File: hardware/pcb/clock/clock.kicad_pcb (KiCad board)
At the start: 2 copper layers, 32 parts, among them J1 01x02_F, J2 01x04_F, SW1 SW_Push, SW2 SW_SPDT, U1 TLC556, U3 74HC02, U4 74HC00

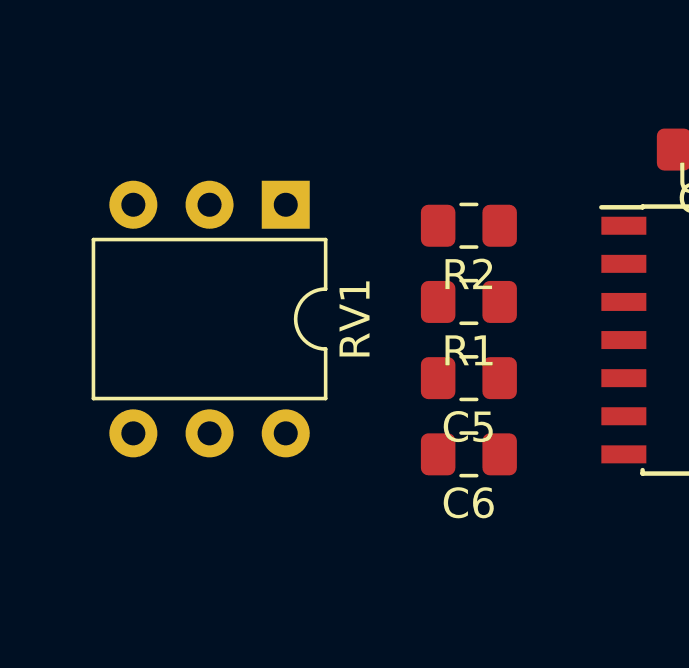
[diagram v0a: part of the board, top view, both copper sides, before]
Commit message: Custom footprints for non-standard parts
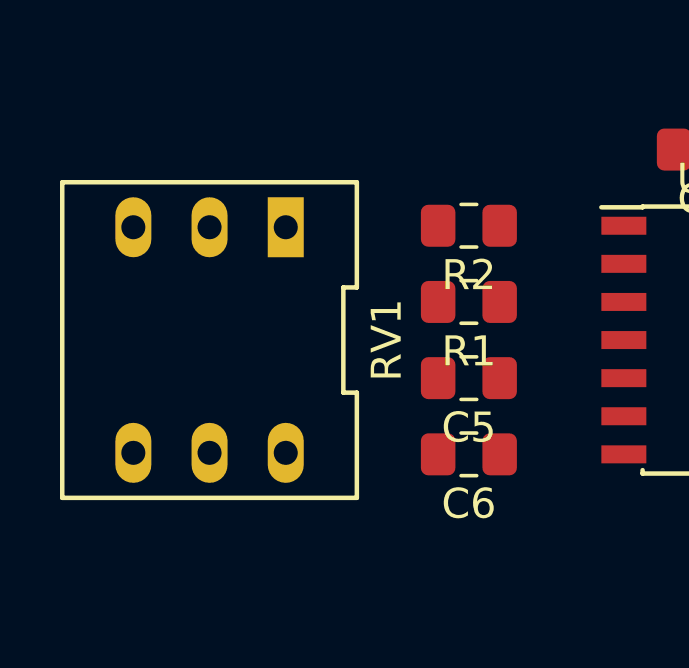
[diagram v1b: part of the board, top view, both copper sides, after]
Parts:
- RV1: footprint Package_DIP:DIP-6_W7.62mm -> clock-custom:POT_DIP_Dual_Vert
- SW2: footprint Custom:SW_Slide_1P2T_CK_OS102011MS2Q -> clock-custom:SW_Slide_1P2T_CK_OS102011MS2Q
- moved RV1 5.18 mm to (30.5, 45.7), turned to 180 degrees
